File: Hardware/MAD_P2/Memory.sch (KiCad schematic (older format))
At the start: 5 parts, among them J5 Micro_SD_Card, U26 W25Q128JVS

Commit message: revising pcb layout
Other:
- moved on the sheet: J5, R11
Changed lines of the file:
@@
 L Connector:Micro_SD_Card J5
 U 1 1 60B0E24B
-P 6150 3300
-F 0 "J5" H 6100 4017 50  0000 C CNN
-F 1 "Micro_SD_Card" H 6100 3926 50  0000 C CNN
-F 2 "Connector_Card:microSD_HC_Hirose_DM3D-SF" H 7300 3600 50  0001 C CNN
-F 3 "http://katalog.we-online.de/em/datasheet/693072010801.pdf" H 6150 3300 50  0001 C CNN
-	1    6150 3300
+P 6150 3350
+F 0 "J5" H 6100 4067 50  0000 C CNN
+F 1 "Micro_SD_Card" H 6100 3976 50  0000 C CNN
+F 2 "Connector_Card:microSD_HC_Hirose_DM3D-SF" H 7300 3650 50  0001 C CNN
+F 3 "http://katalog.we-online.de/em/datasheet/693072010801.pdf" H 6150 3350 50  0001 C CNN
+	1    6150 3350
 	1    0    0    -1
 $EndComp
@@
 L power:+3.3V #PWR0142
 U 1 1 60B14DB5
-P 5250 3300
-F 0 "#PWR0142" H 5250 3150 50  0001 C CNN
-F 1 "+3.3V" V 5265 3428 50  0000 L CNN
-F 2 "" H 5250 3300 50  0001 C CNN
-F 3 "" H 5250 3300 50  0001 C CNN
-	1    5250 3300
+P 5250 3350
+F 0 "#PWR0142" H 5250 3200 50  0001 C CNN
+F 1 "+3.3V" V 5265 3478 50  0000 L CNN
+F 2 "" H 5250 3350 50  0001 C CNN
+F 3 "" H 5250 3350 50  0001 C CNN
+	1    5250 3350
 	0    -1   -1   0
 $EndComp
@@
 L power:GND #PWR0143
 U 1 1 60B15F33
-P 5250 3500
-F 0 "#PWR0143" H 5250 3250 50  0001 C CNN
-F 1 "GND" V 5255 3372 50  0000 R CNN
-F 2 "" H 5250 3500 50  0001 C CNN
-F 3 "" H 5250 3500 50  0001 C CNN
-	1    5250 3500
+P 5250 3550
+F 0 "#PWR0143" H 5250 3300 50  0001 C CNN
+F 1 "GND" V 5255 3422 50  0000 R CNN
+F 2 "" H 5250 3550 50  0001 C CNN
+F 3 "" H 5250 3550 50  0001 C CNN
+	1    5250 3550
 	0    1    1    0
 $EndComp
-NoConn ~ 6950 3900
-Text Label 4550 3100 2    50   ~ 0
+NoConn ~ 6950 3950
+Text Label 4550 3150 2    50   ~ 0
 P60
-Text Label 4550 3200 2    50   ~ 0
+Text Label 4550 3250 2    50   ~ 0
 P59
-Text Label 4550 3400 2    50   ~ 0
+Text Label 4550 3450 2    50   ~ 0
 P61
-Text Label 4550 3600 2    50   ~ 0
+Text Label 4550 3650 2    50   ~ 0
 P58
-NoConn ~ 5250 3700
-NoConn ~ 5250 3000
+NoConn ~ 5250 3750
+NoConn ~ 5250 3050
 $Comp
 L Device:R_Small R11
 U 1 1 60B28350
-P 4750 3600
-F 0 "R11" V 4850 3600 50  0000 C CNN
-F 1 "240R" V 4650 3600 50  0000 C CNN
-F 2 "Resistor_SMD:R_0603_1608Metric" H 4750 3600 50  0001 C CNN
-F 3 "~" H 4750 3600 50  0001 C CNN
-	1    4750 3600
+P 4750 3650
+F 0 "R11" V 4850 3650 50  0000 C CNN
+F 1 "240R" V 4650 3650 50  0000 C CNN
+F 2 "Resistor_SMD:R_0603_1608Metric" H 4750 3650 50  0001 C CNN
+F 3 "~" H 4750 3650 50  0001 C CNN
+	1    4750 3650
 	0    -1   -1   0
 $EndComp
@@
 	7550 5000 7200 5000
 Wire Wire Line
-	4550 3600 4650 3600
+	4550 3650 4650 3650
 Wire Wire Line
-	4850 3600 5250 3600
+	4850 3650 5250 3650
 Wire Wire Line
-	4550 3400 5250 3400
+	4550 3450 5250 3450
 Wire Wire Line
-	4550 3200 5250 3200
+	4550 3250 5250 3250
 Wire Wire Line
-	4550 3100 5250 3100
+	4550 3150 5250 3150
 $Comp
 L Memory_Flash:W25Q128JVS U26
@@
 Text Notes 4750 4550 0    129  ~ 0
 Optional Boot SPI Flash
-Text Notes 5100 2400 0    129  ~ 0
+Text Notes 5100 2450 0    129  ~ 0
 Boot SD Card
 $EndSCHEMATC

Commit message: routed adc
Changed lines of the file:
@@
 $EndComp
 NoConn ~ 6950 3950
-Text Label 4550 3150 2    50   ~ 0
-P60
-Text Label 4550 3250 2    50   ~ 0
-P59
-Text Label 4550 3450 2    50   ~ 0
-P61
-Text Label 4550 3650 2    50   ~ 0
-P58
 NoConn ~ 5250 3750
 NoConn ~ 5250 3050
@@
 	1    0    0    -1
 $EndComp
-Text Label 7550 5000 0    50   ~ 0
-P61
 Wire Wire Line
 	7550 5000 7200 5000
@@
 Text Label 4900 5450 2    50   ~ 0
 P60
-Text Label 5900 5250 0    50   ~ 0
-P58
-Text Label 5900 5150 0    50   ~ 0
-P59
 $Comp
 L power:GND #PWR0148
@@
 Text Notes 5100 2450 0    129  ~ 0
 Boot SD Card
+Text GLabel 4550 3150 0    50   Input ~ 0
+P60
+Text GLabel 4550 3250 0    50   Input ~ 0
+P59
+Text GLabel 4550 3450 0    50   Input ~ 0
+P61
+Text GLabel 4550 3650 0    50   Input ~ 0
+P58
+Text GLabel 5900 5150 2    50   Input ~ 0
+P59
+Text GLabel 5900 5250 2    50   Input ~ 0
+P58
+Text GLabel 7550 5000 2    50   Input ~ 0
+P61
 $EndSCHEMATC

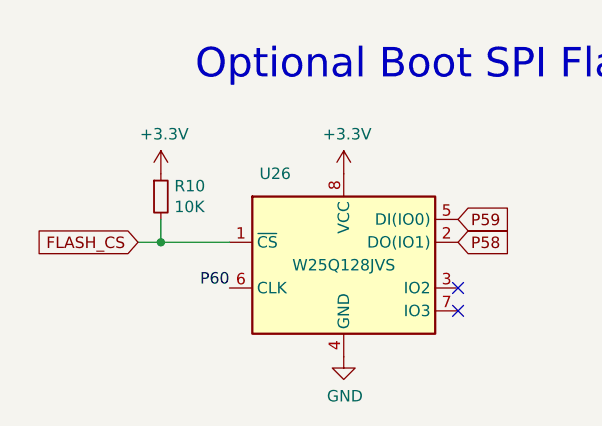
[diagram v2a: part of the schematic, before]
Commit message: fixed DAC issue and added silkscreen
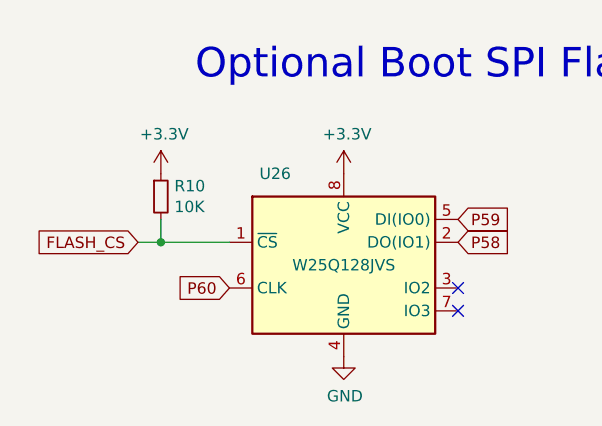
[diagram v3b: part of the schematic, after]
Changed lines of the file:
@@
 Wire Wire Line
 	4500 5250 4600 5250
-Text Label 4900 5450 2    50   ~ 0
-P60
 $Comp
 L power:GND #PWR0148
@@
 Text GLabel 7550 5000 2    50   Input ~ 0
 P61
+Text GLabel 4900 5450 0    50   Input ~ 0
+P60
 $EndSCHEMATC

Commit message: completed BOM with digikey and LSCS parts
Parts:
- J5: DIGIKEY (none) -> 732-3820-2-ND; TYPE (none) -> DIGIKEY
- JP10: TYPE (none) -> NA
- R10: LCSC (none) -> C25804; TYPE (none) -> BASIC
- R11: LCSC (none) -> C23350; TYPE (none) -> BASIC
- U26: LCSC (none) -> C97521; TYPE (none) -> BASIC
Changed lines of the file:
@@
 F 2 "Connector_Card:microSD_HC_Hirose_DM3D-SF" H 7300 3650 50  0001 C CNN
 F 3 "http://katalog.we-online.de/em/datasheet/693072010801.pdf" H 6150 3350 50  0001 C CNN
+F 4 "732-3820-2-ND" H 6150 3350 50  0001 C CNN "DIGIKEY"
+F 5 "DIGIKEY" H 6150 3350 50  0001 C CNN "TYPE"
 	1    6150 3350
 	1    0    0    -1
@@
 F 2 "Resistor_SMD:R_0603_1608Metric" H 4750 3650 50  0001 C CNN
 F 3 "~" H 4750 3650 50  0001 C CNN
+F 4 "C23350" H 4750 3650 50  0001 C CNN "LCSC"
+F 5 "BASIC" H 4750 3650 50  0001 C CNN "TYPE"
 	1    4750 3650
 	0    -1   -1   0
@@
 F 2 "Connector_PinHeader_2.54mm:PinHeader_1x02_P2.54mm_Vertical" H 7100 5000 50  0001 C CNN
 F 3 "~" H 7100 5000 50  0001 C CNN
+F 4 "NA" H 7100 5000 50  0001 C CNN "TYPE"
 	1    7100 5000
 	1    0    0    -1
@@
 F 2 "Package_SO:SOIC-8_5.23x5.23mm_P1.27mm" H 5400 5350 50  0001 C CNN
 F 3 "http://www.winbond.com/resource-files/w25q128jv_dtr%20revc%2003272018%20plus.pdf" H 5400 5350 50  0001 C CNN
+F 4 "C97521" H 5400 5350 50  0001 C CNN "LCSC"
+F 5 "BASIC" H 5400 5350 50  0001 C CNN "TYPE"
 	1    5400 5350
 	1    0    0    -1
@@
 F 2 "Resistor_SMD:R_0603_1608Metric" H 4600 5050 50  0001 C CNN
 F 3 "~" H 4600 5050 50  0001 C CNN
+F 4 "C25804" H 4600 5050 50  0001 C CNN "LCSC"
+F 5 "BASIC" H 4600 5050 50  0001 C CNN "TYPE"
 	1    4600 5050
 	1    0    0    -1

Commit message: updated bom with lcsc part #
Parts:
- J5: LCSC (none) -> C719027; TYPE DIGIKEY -> EXT
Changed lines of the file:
@@
 F 3 "http://katalog.we-online.de/em/datasheet/693072010801.pdf" H 6150 3350 50  0001 C CNN
 F 4 "732-3820-2-ND" H 6150 3350 50  0001 C CNN "DIGIKEY"
-F 5 "DIGIKEY" H 6150 3350 50  0001 C CNN "TYPE"
+F 5 "EXT" H 6150 3350 50  0001 C CNN "TYPE"
+F 6 "C719027" H 6150 3350 50  0001 C CNN "LCSC"
 	1    6150 3350
 	1    0    0    -1

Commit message: added more functionality to JSON for motion quartet, motion set, motion profiles, machine profile, and more
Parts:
- J5: ASSEMBLED (none) -> NO
- R10, R11, U26: ASSEMBLED (none) -> YES
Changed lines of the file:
@@
 F 5 "EXT" H 6150 3350 50  0001 C CNN "TYPE"
 F 6 "C719027" H 6150 3350 50  0001 C CNN "LCSC"
+F 7 "NO" H 6150 3350 50  0001 C CNN "ASSEMBLED"
 	1    6150 3350
 	1    0    0    -1
@@
 F 4 "C23350" H 4750 3650 50  0001 C CNN "LCSC"
 F 5 "BASIC" H 4750 3650 50  0001 C CNN "TYPE"
+F 6 "YES" H 4750 3650 50  0001 C CNN "ASSEMBLED"
 	1    4750 3650
 	0    -1   -1   0
@@
 F 4 "C97521" H 5400 5350 50  0001 C CNN "LCSC"
 F 5 "BASIC" H 5400 5350 50  0001 C CNN "TYPE"
+F 6 "YES" H 5400 5350 50  0001 C CNN "ASSEMBLED"
 	1    5400 5350
 	1    0    0    -1
@@
 F 4 "C25804" H 4600 5050 50  0001 C CNN "LCSC"
 F 5 "BASIC" H 4600 5050 50  0001 C CNN "TYPE"
+F 6 "YES" H 4600 5050 50  0001 C CNN "ASSEMBLED"
 	1    4600 5050
 	1    0    0    -1
